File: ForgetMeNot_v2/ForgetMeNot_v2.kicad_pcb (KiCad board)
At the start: 4 copper layers, 16 x 33 mm, 44 parts, among them J1 Conn_01x04, SW1 SW_Push, U1 RP2040, U2 W25Q128JVS, U4 LIS2HH12, U5 MCP1640x-xMC, Y1 Crystal_ABM8

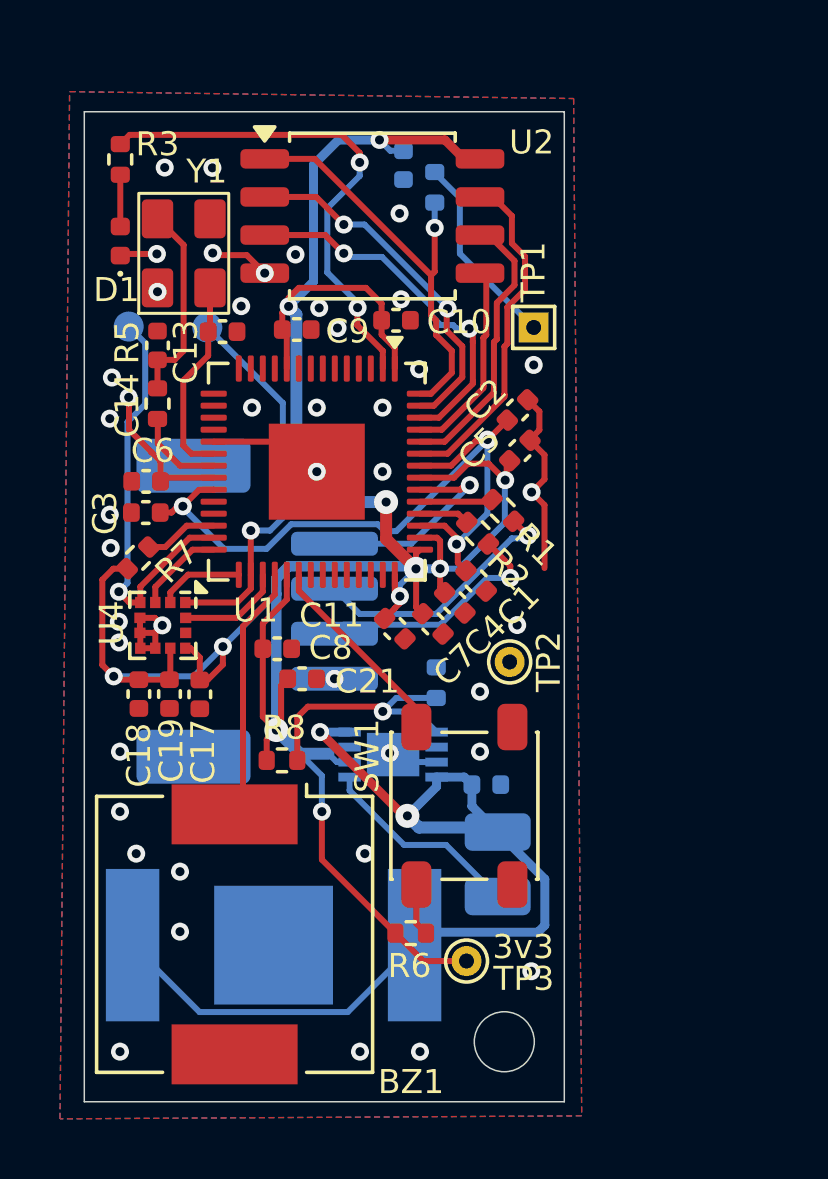
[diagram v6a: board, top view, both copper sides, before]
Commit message: updated MCU from RP2040 to ATmega328p
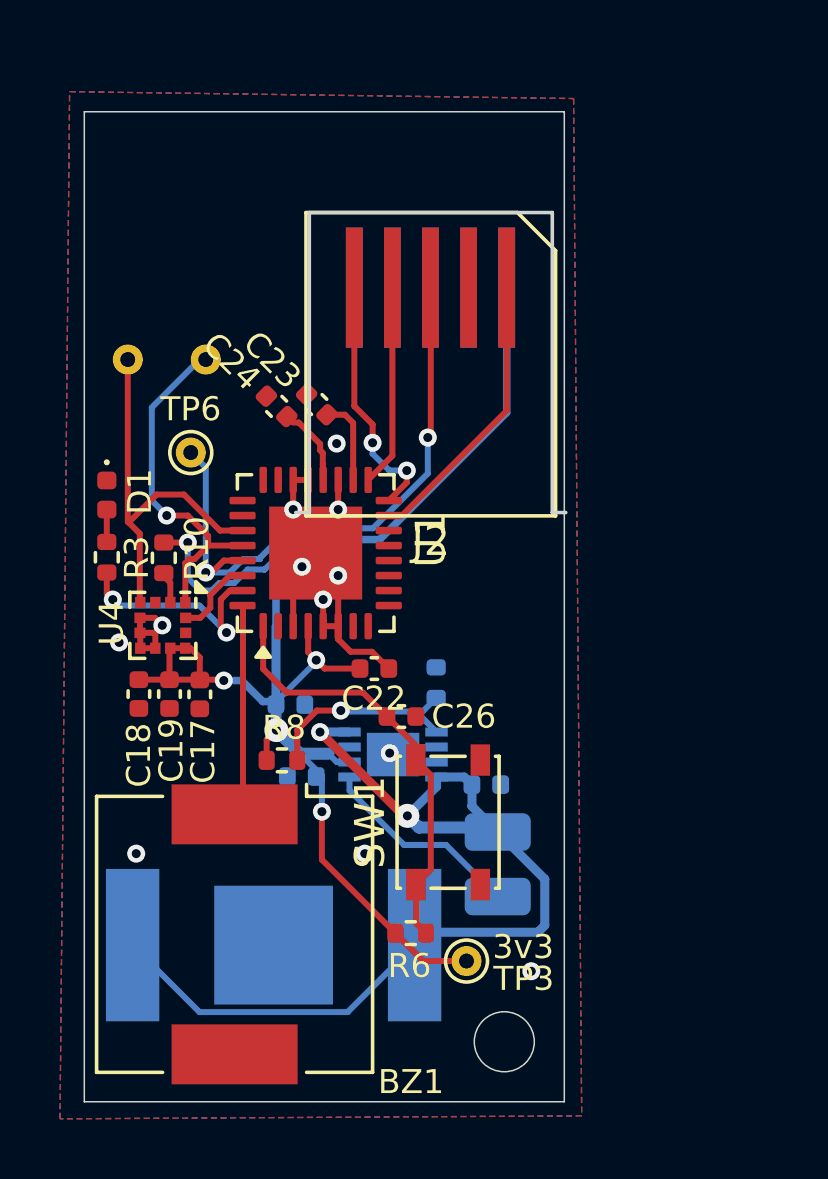
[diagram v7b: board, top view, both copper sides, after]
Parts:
- removed C1, C4: 1u, Capacitor_SMD:C_0402_1005Metric
- removed C10, C11, C12, C2, C3, C5, C6, C7, C8, C9: 100n, Capacitor_SMD:C_0402_1005Metric
- removed C13, C14: 15p, Capacitor_SMD:C_0402_1005Metric
- removed J1: Conn_01x04, Connector_Molex:Molex_CLIK-Mate_502585-0470_1x04-1MP_P1.50mm_Horizontal
- removed R1, R2: 27.4, Resistor_SMD:R_0402_1005Metric
- removed R4, R5: 1k, Resistor_SMD:R_0402_1005Metric
- removed R7: 10k, Resistor_SMD:R_0402_1005Metric
- removed TP1: BOOT, TestPoint:TestPoint_THTPad_1.0x1.0mm_Drill0.5mm
- removed TP2: BOOT, TestPoint:TestPoint_THTPad_D1.0mm_Drill0.5mm
- removed U2: W25Q128JVS, Package_SO:SOIC-8_5.3x5.3mm_P1.27mm
- removed Y1: Crystal_ABM8, Crystal:ABM8
- added C22: 100nF, Capacitor_SMD:C_0402_1005Metric, F.Cu at (140.3, 96.8)
- added C23: 100nF, Capacitor_SMD:C_0402_1005Metric, F.Cu at (138.4, 88.0)
- added C24: 100nF, Capacitor_SMD:C_0402_1005Metric, F.Cu at (137.1, 88.1)
- added C25: 10uF, Capacitor_SMD:C_0402_1005Metric, B.Cu at (137.5, 98.0)
- added C26: 100nF, Capacitor_SMD:C_0402_1005Metric, F.Cu at (141.2, 98.4)
- added J2: ISP Connector, Connector_PCBEdge:Samtec_MECF-05-0_-NP-L-DV_2x05_P1.27mm_Edge, F.Cu at (142.2, 86.6)
- added R10: 10k, Resistor_SMD:R_0402_1005Metric, F.Cu at (133.3, 93.1)
- added TP6: RST, TestPoint:TestPoint_THTPad_D1.0mm_Drill0.5mm, F.Cu at (134.2, 89.6)
- C21: moved to B.Cu
- R3: value 220 -> 200
- SW1: footprint Button_Switch_SMD:SW_SPST_PTS647_Sx38 -> Button_Switch_SMD:SW_SPST_PTS810
- TP4, TP5: footprint TestPoint:TestPoint_Pad_D1.0mm -> TestPoint:TestPoint_THTPad_D1.0mm_Drill0.5mm
- U1: value RP2040 -> ATmega328PB-M; footprint Package_DFN_QFN:QFN-56-1EP_7x7mm_P0.4mm_EP3.2x3.2mm -> Package_DFN_QFN:QFN-32-1EP_5x5mm_P0.5mm_EP3.1x3.1mm
- moved R3 13.3 mm to (131.4, 93.1), turned to 90 degrees
- moved D1 8.48 mm to (131.4, 91.0), turned to -90 degrees
- moved C21 3.26 mm to (137.9, 100.4)
- moved U1 2.71 mm to (138.4, 93.0), turned to 90 degrees
- moved TP4 1.10 mm to (132.1, 86.5)
- moved TP5 1.07 mm to (134.7, 86.5)
- moved SW1 0.77 mm to (142.8, 101.9)
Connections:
- net /ACC_SDA renamed ACC_SDA
- net /BUZZ renamed BUZZ
- C17 pad 2: +3.3V -> VCC
- C18 pad 2: +3.3V -> VCC
- C19 pad 2: +3.3V -> VCC
- C21 pad 1: +3.3V -> GND
- C21 pad 2: GND -> VCC
- R3 pad 1: /LED -> LED
- R6 pad 1: +3.3V -> VCC
- R6 pad 2: /ZERO -> ZERO
- R8 pad 1: +3.3V -> VCC
- SW1 pad 1: /ZERO -> ZERO
- TP3 pad 1: +3.3V -> VCC
- TP5 pad 1: /ACC_SCL -> ACC_SCL
- U1 pad 1: +3.3V -> ZERO
- U1 pad 10: +3.3V -> unconnected-(U1-PD6-Pad10)
- U1 pad 15: unconnected-(U1-GPIO12-Pad15) -> MOSI
- U1 pad 16: unconnected-(U1-GPIO13-Pad16) -> MISO
- U1 pad 17: unconnected-(U1-GPIO14-Pad17) -> SCK
- U1 pad 18: unconnected-(U1-GPIO15-Pad18) -> VCC
- U1 pad 2: /LED -> unconnected-(U1-PD4-Pad2)
- U1 pad 20: Net-(U1-XIN) -> VCC
- U1 pad 21: Net-(U1-XOUT) -> GND
- U1 pad 22: +3.3V -> GND
- U1 pad 23: +1V1 -> unconnected-(U1-PC0-Pad23)
- U1 pad 26: Net-(U1-RUN) -> unconnected-(U1-PC3-Pad26)
- U1 pad 28: /ACC_SDO -> ACC_SCL
- U1 pad 29: /ACC_CS -> RESET
- U1 pad 3: unconnected-(U1-GPIO1-Pad3) -> GND
- U1 pad 30: /ACC_SCL -> ACC_INT
- U1 pad 31: /ACC_INT -> LED
- U1 pad 33: +3.3V -> GND
- U1 pad 4: unconnected-(U1-GPIO2-Pad4) -> VCC
- U1 pad 5: unconnected-(U1-GPIO3-Pad5) -> GND
- U1 pad 6: unconnected-(U1-GPIO4-Pad6) -> GND
- U4 pad 1: /ACC_SCL -> ACC_SCL
- U4 pad 10: +3.3V -> VCC
- U4 pad 12: /ACC_INT -> ACC_INT
- U4 pad 2: /ACC_CS -> Net-(U4-~{CS})
- U4 pad 3: /ACC_SDO -> unconnected-(U4-SA0/SDO-Pad3)
- U4 pad 9: +3.3V -> VCC
- U5 pad 6: +3.3V -> VCC
- U5 pad 7: +3.3V -> VCC
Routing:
- net +3.3V: track 105.0 -> 0.00 mm, vias 12 -> 0
- net VCC: track 0.00 -> 59.8 mm, vias 0 -> 5
- net +1V1: track 24.7 -> 0.00 mm, vias 3 -> 0
- net RESET: track 0.00 -> 20.6 mm, vias 0 -> 2
- net /LED: track 16.8 -> 0.00 mm, vias 2 -> 0
- net /QSPI_SS: track 14.7 -> 0.00 mm, vias 1 -> 0
- net ZERO: track 0.00 -> 14.4 mm
- net /ACC_SCL: track 12.9 -> 0.00 mm, vias 1 -> 0
- net /QSPI_SD2: track 12.4 -> 0.00 mm, vias 2 -> 0
- net /QSPI_SD1: track 12.0 -> 0.00 mm, vias 2 -> 0
- net ACC_SCL: track 0.00 -> 11.7 mm, vias 0 -> 1
- net /QSPI_SD3: track 11.4 -> 0.00 mm
- net /QSPI_SCLK: track 9.99 -> 0.00 mm
- net MOSI: track 0.00 -> 9.48 mm
- net /USB D+: track 8.70 -> 0.00 mm, vias 1 -> 0
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
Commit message: changed connector
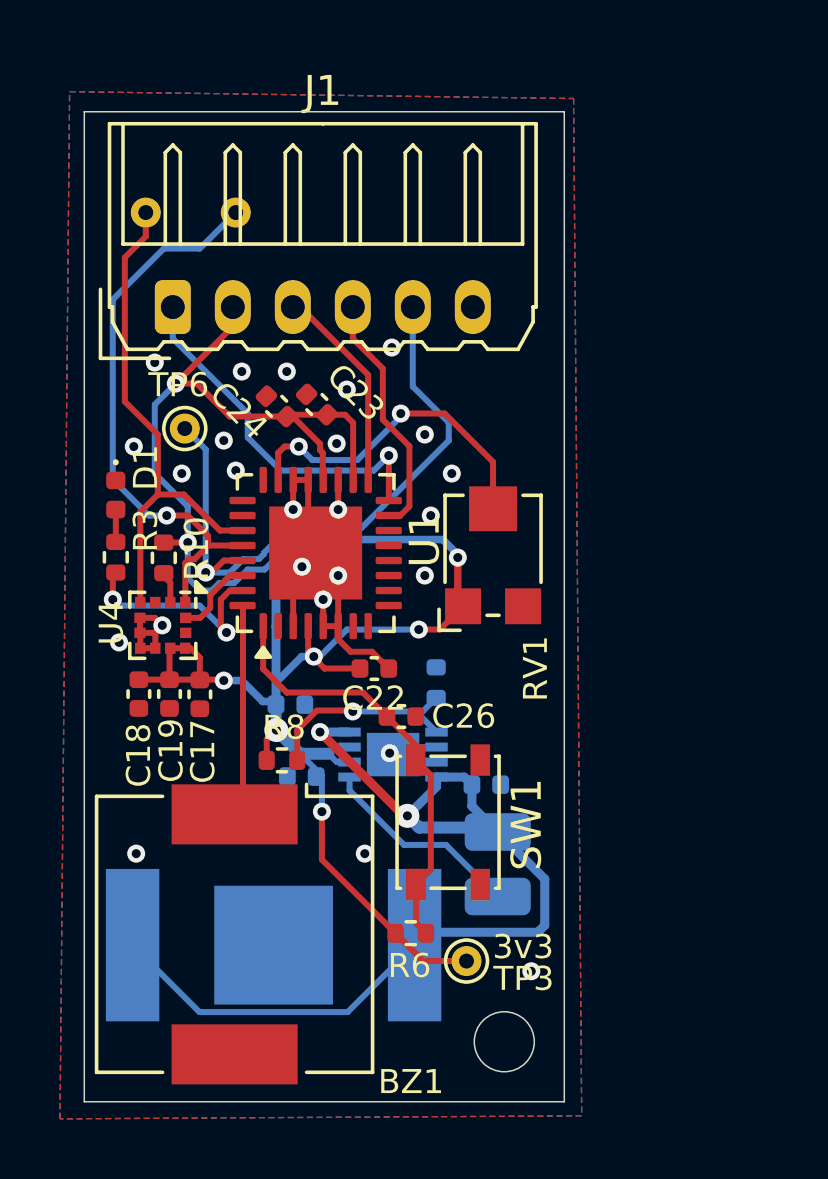
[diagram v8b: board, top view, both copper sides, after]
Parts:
- removed J2: ISP Connector, Connector_PCBEdge:Samtec_MECF-05-0_-NP-L-DV_2x05_P1.27mm_Edge
- added J1: ISP Connector, Connector_Molex:Molex_Micro-Latch_53254-0670_1x06_P2.00mm_Horizontal, F.Cu at (133.6, 84.8)
- added RV1: R_Potentiometer_Trim, Potentiometer_SMD:Potentiometer_Bourns_TC33X_Vertical, F.Cu at (144.3, 92.9)
- moved TP5 5.00 mm to (135.7, 81.6)
- moved TP4 4.94 mm to (132.7, 81.6)
- moved TP6 0.82 mm to (134.0, 88.8)
- moved D1 0.30 mm to (131.7, 91.0)
- moved R3 0.30 mm to (131.7, 93.1)
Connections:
- U1 pad 23: unconnected-(U1-PC0-Pad23) -> POT
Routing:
- net VCC: track 59.8 -> 75.2 mm, vias 5 -> 8
- net POT: track 0.00 -> 11.3 mm, vias 0 -> 2
- net ACC_SCL: track 11.7 -> 19.0 mm
- net ACC_SDA: track 12.9 -> 17.6 mm
- net MISO: track 8.41 -> 12.2 mm, vias 2 -> 1
- net Net-(U5-V_{FB}): track 8.51 -> 7.08 mm
- net MOSI: track 9.48 -> 8.24 mm
- net RESET: track 20.6 -> 21.8 mm, vias 2 -> 1
- net GND: vias 12 -> 25
